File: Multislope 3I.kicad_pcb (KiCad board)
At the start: 4 copper layers, 112.5 x 56 mm, 115 parts, among them J1 INT, J10 SLOT, J11 TEST, J12 UART, J13 INPUT, J2 TEST, J3 SLOT, J4 SLOT, J5 SLOT, J6 SLOT, J7 SLOT, J8 SLOT, J9 SLOT, Q1 5551, U1 OPA21xx, U10 LM311, U11 NE5534, U12 OPA197, U13 431, U14 431, U15 MCP3202, U16 Pico, U17 LM35, U18 ADuM121N, U2 LM399, U3 CD4053B, U4 OPA1xx, U5 OPA1xx, U6 OPA1xx, U7 431, U8 431, U9 408

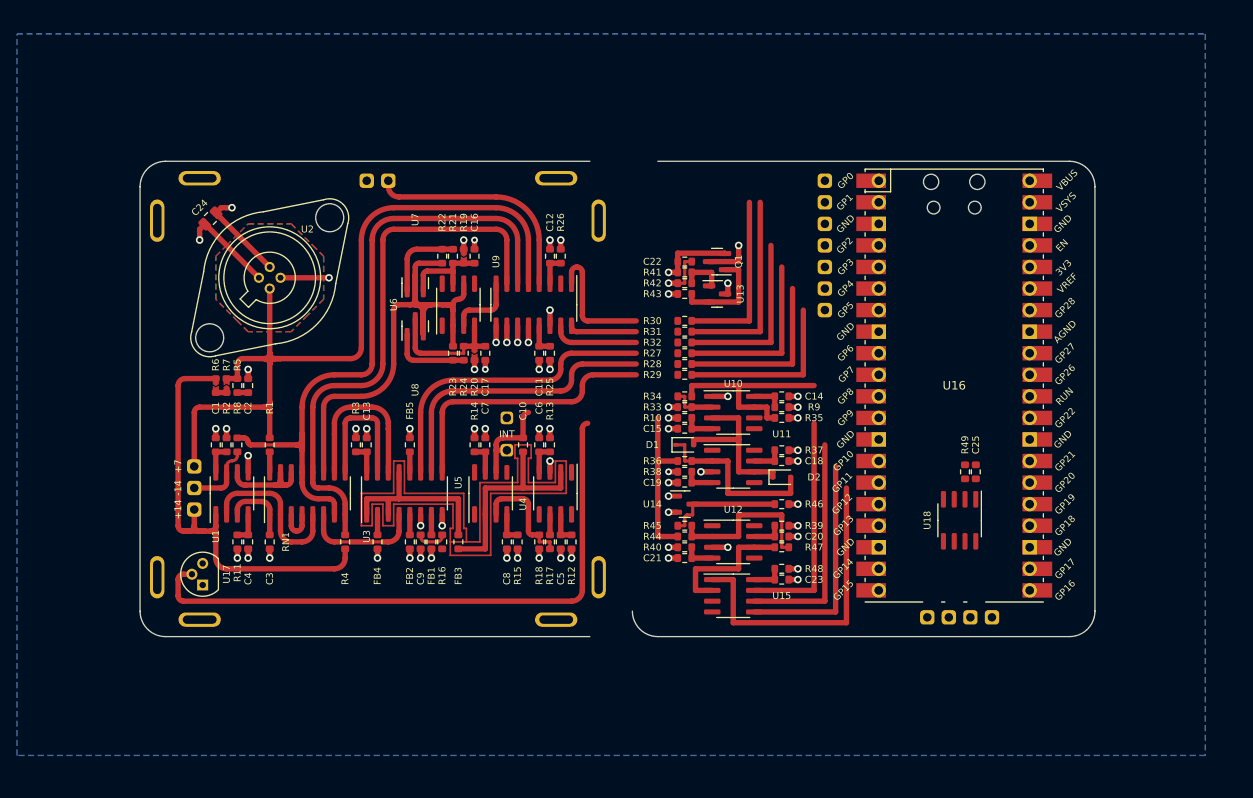
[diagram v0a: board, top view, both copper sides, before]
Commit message: PCB compact-ified
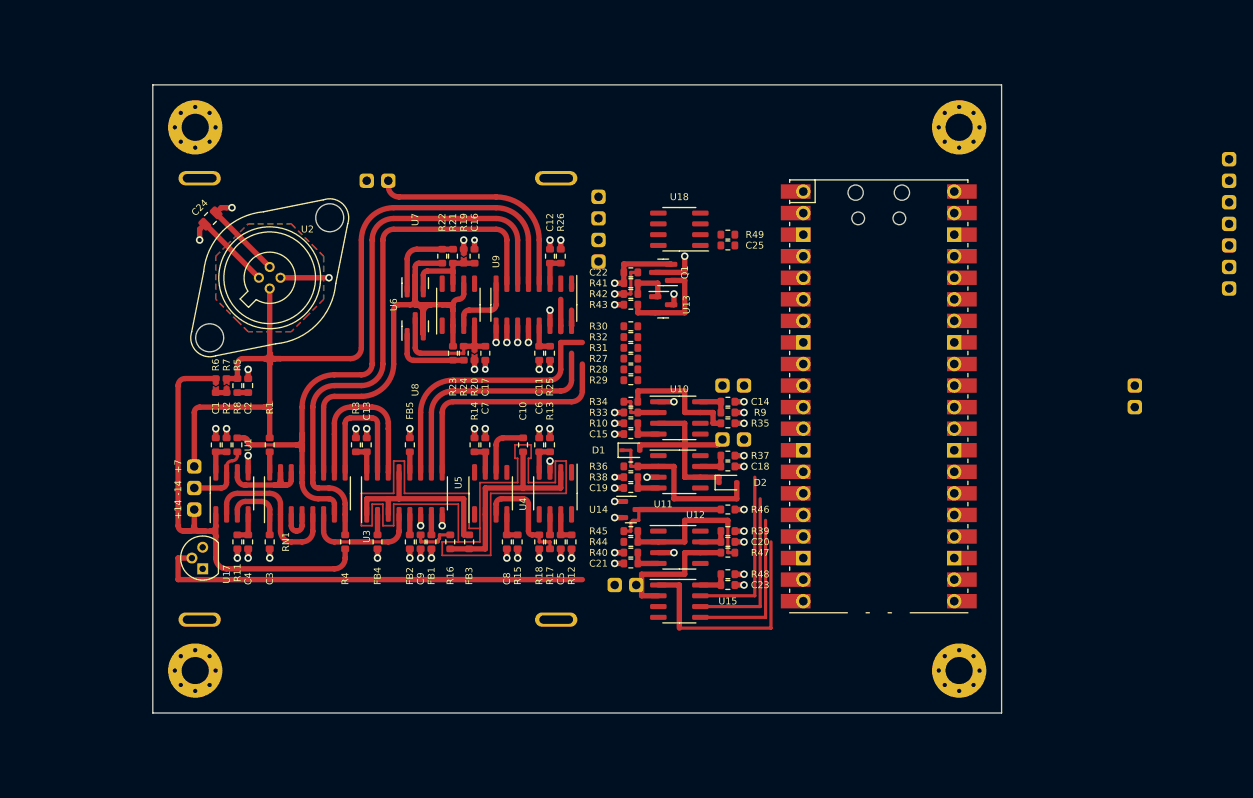
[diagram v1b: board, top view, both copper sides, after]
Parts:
- removed J10, J8: SLOT, Connector_PinHeader_2.54mm:PinHeader_1x01_P2.54mm_Vertical
- added H1: MountingHole, MountingHole:MountingHole_3.2mm_M3_Pad_Via, F.Cu at (186.0, 132.0)
- added H2: MountingHole, MountingHole:MountingHole_3.2mm_M3_Pad_Via, F.Cu at (96.0, 132.0)
- added H3: MountingHole, MountingHole:MountingHole_3.2mm_M3_Pad_Via, F.Cu at (186.0, 68.0)
- added H4: MountingHole, MountingHole:MountingHole_3.2mm_M3_Pad_Via, F.Cu at (96.0, 68.0)
- added J14: SLOPE, Connector_PinHeader_2.54mm:PinHeader_1x02_P2.54mm_Vertical, F.Cu at (158.1, 104.8)
- J1: footprint Connector_PinHeader_2.54mm:PinHeader_1x03_P2.54mm_Vertical -> Connector_PinHeader_2.54mm:PinHeader_1x02_P2.54mm_Vertical
- J3: value SLOT -> COMP; footprint Connector_PinHeader_2.54mm:PinHeader_1x01_P2.54mm_Vertical -> Connector_PinHeader_2.54mm:PinHeader_1x02_P2.54mm_Vertical
- J7: value SLOT -> SLOPE2; footprint Connector_PinHeader_2.54mm:PinHeader_1x01_P2.54mm_Vertical -> Connector_PinHeader_2.54mm:PinHeader_1x02_P2.54mm_Vertical
- R44: value 5K -> 50K
- R45: value 2K5 -> 25K
- R47: value 1K5 -> 15K
- moved J1 74.4 mm to (206.7, 98.4), turned to 0 degrees
- moved J3 69.4 mm to (158.1, 98.4)
- moved J12 62.5 mm to (143.5, 83.8), turned to 180 degrees
- moved J2 47.7 mm to (217.8, 71.8)
- moved U18 47.6 mm to (153.0, 80.0), turned to 180 degrees
- moved J7 43.1 mm to (148.0, 121.9), turned to -90 degrees
- moved C25 39.6 mm to (158.8, 81.9), turned to 180 degrees
- moved R49 39.5 mm to (158.8, 80.6), turned to 0 degrees
- moved U16 8.98 mm to (176.5, 99.7)
- moved R31 6.63 mm to (147.3, 94.0)
- moved C22 6.48 mm to (147.3, 85.1)
- moved Q1 6.48 mm to (151.1, 85.1)
- moved R43 6.48 mm to (147.3, 88.9)
- moved U13 6.48 mm to (151.1, 88.9)
- moved R41 6.48 mm to (147.3, 86.4)
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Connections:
- net Net-(D1-Pad2) renamed /SLOPE
- J2 pad 2: Net-(J2-Pad2) -> Net-(U16-Pad4)
- J2 pad 4: Net-(J2-Pad4) -> Net-(U16-Pad2)
- J3 pad 1: GND -> /COMP
- J7 pad 1: GND -> /SLOPE2
- R31 pad 2: Net-(J2-Pad2) -> Net-(U16-Pad4)
- R32 pad 2: Net-(J2-Pad4) -> Net-(U16-Pad2)
- R34 pad 2: Net-(R34-Pad2) -> /COMP
- R35 pad 1: Net-(R34-Pad2) -> /COMP
- R47 pad 2: Net-(R47-Pad2) -> /SLOPE2
- U10 pad 7: Net-(R34-Pad2) -> /COMP
- U12 pad 6: Net-(R47-Pad2) -> /SLOPE2
- U15 pad 2: Net-(R47-Pad2) -> /SLOPE2
- U16 pad 12: Net-(R34-Pad2) -> /COMP
- U16 pad 2: Net-(J2-Pad2) -> Net-(U16-Pad2)
- U16 pad 4: Net-(J2-Pad4) -> Net-(U16-Pad4)
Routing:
- net /SLOPE: track 21.3 -> 75.0 mm
- net /SLOPE2: track 0.00 -> 50.7 mm
- net +15V: track 206.7 -> 157.8 mm
- net -15V: track 253.9 -> 219.6 mm
- net Net-(R34-Pad2): track 23.7 -> 0.00 mm
- net Net-(J2-Pad2): track 23.3 -> 0.00 mm
- net /INT: track 30.1 -> 6.85 mm
- net Net-(J2-Pad6): track 20.8 -> 0.00 mm
- net Net-(J2-Pad4): track 20.8 -> 0.00 mm
- net Net-(J2-Pad1): track 20.8 -> 0.00 mm
- net Net-(J2-Pad7): track 20.8 -> 0.00 mm
- net Net-(J2-Pad5): track 20.8 -> 0.00 mm
- net Net-(U15-Pad3): track 72.5 -> 51.8 mm
- net Net-(R47-Pad2): track 16.4 -> 0.00 mm
- net /COMP: track 0.00 -> 14.9 mm
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- removed copper zone on B.Cu, net GND
- removed copper zone on In2.Cu, net GND
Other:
- board size 112.5 x 56 mm -> 100 x 74 mm

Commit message: removed redundant files
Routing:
- net /SLOPE: track 75.0 -> 26.1 mm
- net /SLOPE2: track 50.7 -> 16.4 mm
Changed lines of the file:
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@@
   (segment (start 153.67 109.22) (end 155.51 109.22) (width 0.635) (layer "F.Cu") (net 65))
   (arc (start 157.48 105.41) (mid 157.929013 105.224013) (end 158.115 104.775) (width 0.635) (layer "F.Cu") (net 65))
-  (segment (start 153.67 106.045) (end 160.655 106.045) (width 0.635) (layer "In1.Cu") (net 65))
-  (segment (start 153.67 90.17) (end 153.67 100.965) (width 0.635) (layer "In1.Cu") (net 65))
-  (segment (start 145.415 90.17) (end 153.67 90.17) (width 0.635) (layer "In1.Cu") (net 65))
-  (segment (start 153.67 100.965) (end 160.655 100.965) (width 0.635) (layer "In1.Cu") (net 65))
-  (segment (start 145.415 90.17) (end 145.415 87.63) (width 0.635) (layer "In1.Cu") (net 65))
-  (segment (start 153.67 100.965) (end 153.67 106.045) (width 0.635) (layer "In1.Cu") (net 65))
-  (segment (start 153.67 90.17) (end 153.67 81.915) (width 0.635) (layer "In1.Cu") (net 65))
   (segment (start 148.145 101.6) (end 150.56 101.6) (width 0.635) (layer "F.Cu") (net 66))
   (segment (start 146.495 100.33) (end 147.32 100.33) (width 0.381) (layer "F.Cu") (net 66))
@@
   (segment (start 155.51 118.11) (end 153.67 118.11) (width 0.635) (layer "F.Cu") (net 124))
   (segment (start 148.59 123.19) (end 150.56 123.19) (width 0.635) (layer "F.Cu") (net 124))
-  (segment (start 147.32 102.235) (end 147.32 108.585) (width 0.635) (layer "In1.Cu") (net 124))
-  (segment (start 145.415 102.235) (end 147.32 102.235) (width 0.635) (layer "In1.Cu") (net 124))
-  (segment (start 147.32 108.585) (end 145.415 108.585) (width 0.635) (layer "In1.Cu") (net 124))
-  (segment (start 145.415 117.475) (end 147.32 117.475) (width 0.635) (layer "In1.Cu") (net 124))
-  (segment (start 147.32 117.475) (end 147.32 112.395) (width 0.635) (layer "In1.Cu") (net 124))
-  (segment (start 160.655 112.395) (end 147.32 112.395) (width 0.635) (layer "In1.Cu") (net 124))
-  (segment (start 147.32 112.395) (end 147.32 108.585) (width 0.635) (layer "In1.Cu") (net 124))
   (segment (start 93.98 118.745) (end 93.98 121.285) (width 0.635) (layer "F.Cu") (net 125))
   (segment (start 95.61 118.745) (end 93.98 118.745) (width 0.635) (layer "F.Cu") (net 125))

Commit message: pcb completed
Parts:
- added C26: 1uf, Resistor_SMD:R_0603_1608Metric, F.Cu at (177.8, 118.7)
- added J10: PWR, Connector_PinHeader_2.54mm:PinHeader_1x04_P2.54mm_Vertical, F.Cu at (166.1, 127.3)
- added J8: PWR, Connector_PinHeader_2.54mm:PinHeader_1x03_P2.54mm_Vertical, F.Cu at (158.1, 67.9)
- R41: value 10R -> 2K4
- R42: value 10R -> 7K5
- R43: value 10R -> 10K
- moved J1 62.0 mm to (145.4, 108.0), turned to 90 degrees
- moved J2 57.3 mm to (160.7, 75.6)
- moved J12 50.0 mm to (181.6, 116.2), turned to -90 degrees
- moved U18 38.3 mm to (177.8, 109.2), turned to -90 degrees
- moved R49 30.2 mm to (178.4, 103.5), turned to 90 degrees
- moved C25 30.1 mm to (179.7, 103.5), turned to -90 degrees
- moved C22 6.98 mm to (147.3, 78.1)
- moved Q1 6.98 mm to (151.1, 78.1)
- moved R41 6.98 mm to (147.3, 79.4)
- moved R42 6.98 mm to (147.3, 80.6)
- moved R43 6.98 mm to (147.3, 81.9)
- moved U13 6.98 mm to (151.1, 81.9)
- moved J13 6.48 mm to (117.5, 67.9)
- moved U14 6.29 mm to (151.8, 108.6)
- moved C15 4.45 mm to (147.3, 99.7)
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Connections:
- J2 pad 2: Net-(U16-Pad4) -> Net-(J2-Pad2)
- J2 pad 4: Net-(U16-Pad2) -> Net-(R31-Pad2)
- R31 pad 2: Net-(U16-Pad4) -> Net-(R31-Pad2)
- R32 pad 2: Net-(U16-Pad2) -> Net-(J2-Pad2)
- U16 pad 11: unconnected-(U16-Pad11) -> Net-(U16-Pad11)
- U16 pad 12: /COMP -> Net-(U18-Pad2)
- U16 pad 13: unconnected-(U16-Pad13) -> GND
- U16 pad 18: unconnected-(U16-Pad18) -> GND
- U16 pad 2: Net-(U16-Pad2) -> Net-(J2-Pad2)
- U16 pad 21: Net-(U16-Pad21) -> unconnected-(U16-Pad21)
- U16 pad 22: Net-(U16-Pad22) -> unconnected-(U16-Pad22)
- U16 pad 23: unconnected-(U16-Pad23) -> GND
- U16 pad 28: unconnected-(U16-Pad28) -> GND
- U16 pad 3: unconnected-(U16-Pad3) -> GND
- U16 pad 33: unconnected-(U16-Pad33) -> GND
- U16 pad 38: unconnected-(U16-Pad38) -> GND
- U16 pad 4: Net-(U16-Pad4) -> Net-(R31-Pad2)
- U16 pad 8: unconnected-(U16-Pad8) -> GND
- U16 pad 9: unconnected-(U16-Pad9) -> /COMP
- U18 pad 2: Net-(U16-Pad22) -> Net-(U18-Pad2)
- U18 pad 3: Net-(U16-Pad21) -> Net-(U16-Pad11)
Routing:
- net +3V3: track 13.3 -> 255.5 mm, vias 5 -> 6
- net +15V: track 157.8 -> 278.0 mm
- net -15V: track 219.6 -> 319.9 mm
- net (no net): track 0.00 -> 48.3 mm
- net /INT: track 6.85 -> 34.0 mm
- net Net-(J2-Pad1): track 0.00 -> 27.0 mm
- net Net-(J2-Pad2): track 0.00 -> 26.2 mm
- net Net-(R31-Pad2): track 0.00 -> 23.1 mm
- net Net-(J2-Pad5): track 0.00 -> 22.6 mm
- net /COMP: track 14.9 -> 37.2 mm
- net Net-(J2-Pad6): track 0.00 -> 22.1 mm
- net Net-(J2-Pad7): track 0.00 -> 21.6 mm
- net Net-(U18-Pad2): track 0.00 -> 15.3 mm
- net Net-(U16-Pad11): track 0.00 -> 13.4 mm
- net GND: track 178.1 -> 189.5 mm, vias 44 -> 46
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- added copper zone on B.Cu, net GND
- added copper zone on In1.Cu, net GND
- added copper zone on In2.Cu, net GND
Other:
- outline, holes or cut-outs redrawn
- board text added: "+15"
- board text added: "+3.3V"
- board text added: "-15"
- board text added: "GND"
- board text added: "IN"
- board text added: "NNNI 1722 Multislope 3I"
- board text added: "RX"
- board text added: "TX"
- board text added: "VCC"

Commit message: 'final' PCB
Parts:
- added C27: 1uf, Resistor_SMD:R_0603_1608Metric, F.Cu at (175.9, 91.4)
- added Q2: 5551, Package_TO_SOT_SMD:SOT-23, F.Cu at (179.7, 91.4)
- added R50: 10K, Resistor_SMD:R_0603_1608Metric, F.Cu at (175.9, 92.7)
- added R51: 10K, Resistor_SMD:R_0603_1608Metric, F.Cu at (175.9, 94.0)
- added R52: 10K, Resistor_SMD:R_0603_1608Metric, F.Cu at (175.9, 95.2)
- added U19: 431, Package_TO_SOT_SMD:SOT-23, F.Cu at (179.7, 95.2)
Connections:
- U16 pad 39: unconnected-(U16-Pad39) -> +5V
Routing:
- net +15V: track 278.0 -> 367.7 mm, vias 10 -> 12
- net -15V: track 319.9 -> 345.5 mm
- net +5V: track 0.00 -> 25.1 mm
- net +3V3: track 255.5 -> 279.9 mm
- net Net-(Q2-Pad1): track 0.00 -> 10.6 mm
- net GND: track 189.5 -> 196.4 mm, vias 46 -> 48
- net Net-(R50-Pad1): track 0.00 -> 5.07 mm
- added copper zone on In1.Cu, net (none)
- added copper zone on In2.Cu, net (none)
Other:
- board text added: "."

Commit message: minor mistakes fixed
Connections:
- J8 pad 1: unconnected-(J8-Pad1) -> +15V
- J8 pad 3: unconnected-(J8-Pad3) -> -15V
- U9 pad 2: unconnected-(U9-Pad2) -> +3V3
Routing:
- net +3V3: track 279.9 -> 292.1 mm, vias 6 -> 7

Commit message: pcb final touches
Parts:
- removed Q1, Q2: 5551, Package_TO_SOT_SMD:SOT-23
- removed R41: 2K4, Resistor_SMD:R_0603_1608Metric
- removed R42: 7K5, Resistor_SMD:R_0603_1608Metric
- removed R43, R50, R51, R52: 10K, Resistor_SMD:R_0603_1608Metric
- removed U13, U19: 431, Package_TO_SOT_SMD:SOT-23
- added C28: 1uf, Resistor_SMD:R_0603_1608Metric, F.Cu at (150.5, 83.2)
- added C29: 1uf, Resistor_SMD:R_0603_1608Metric, F.Cu at (150.5, 81.9)
- added C30: 1uf, Resistor_SMD:R_0603_1608Metric, F.Cu at (99.7, 116.8)
- added J15: PWR, Connector_PinHeader_2.54mm:PinHeader_1x03_P2.54mm_Vertical, F.Cu at (153.0, 73.7)
- added SW1: RST, Button_Switch_SMD:SW_Push_1P1T_NO_CK_KMR2, F.Cu at (164.5, 70.5)
- added U20: HT7533, Package_TO_SOT_SMD:SOT-89-3, F.Cu at (146.4, 78.1)
- added U21: HT7550, Package_TO_SOT_SMD:SOT-89-3, F.Cu at (146.4, 83.2)
- moved C27 29.3 mm to (150.5, 76.8)
- moved J2 3.81 mm to (164.5, 75.6)
- moved C22 3.18 mm to (150.5, 78.1)
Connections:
- C22 pad 1: +3V3 -> +15V
- C27 pad 1: +5V -> +3V3
- U16 pad 30: unconnected-(U16-Pad30) -> Net-(SW1-Pad2)
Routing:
- net +3V3: track 292.1 -> 442.4 mm, vias 7 -> 8
- net +15V: track 367.7 -> 290.4 mm, vias 12 -> 24
- net Net-(SW1-Pad2): track 0.00 -> 54.8 mm, vias 0 -> 1
- net +5V: track 25.1 -> 60.2 mm, vias 0 -> 1
- net -15V: track 345.5 -> 358.2 mm
- net Net-(Q1-Pad1): track 10.6 -> 0.00 mm
- net Net-(Q2-Pad1): track 10.6 -> 0.00 mm
- net Net-(R41-Pad1): track 5.21 -> 0.00 mm
- net Net-(R50-Pad1): track 5.07 -> 0.00 mm
- net GND: track 196.4 -> 199.1 mm, vias 48 -> 52
- net Net-(J2-Pad1): track 27.0 -> 25.2 mm
- net Net-(J2-Pad2): track 26.2 -> 24.7 mm
- added copper zone on B.Cu, net +15V
- added copper zone on F.Cu, net +15V
- added copper zone on In1.Cu, net +15V
- added copper zone on In2.Cu, net +15V
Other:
- board text added: "+3V3"
- board text added: "+5V"

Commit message: Changes
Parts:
- added R41: 0R, 0603 Jumper:0603 Jumper, F.Cu at (147.3, 118.7)
- added R42: 0R, 0603 Jumper:0603 Jumper, F.Cu at (147.3, 120.0)
- R44: value 50K -> 51K
- R45: value 25K -> 24K
- moved J7 0.63 mm to (148.0, 116.8)
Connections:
- net Net-(R27-Pad1) renamed /PWMA
- net Net-(R28-Pad1) renamed /PWMB
- net Net-(R29-Pad1) renamed /MEAS
- U15 pad 2: /SLOPE2 -> Net-(U15-Pad2)
- U15 pad 5: Net-(U15-Pad5) -> Net-(U16-Pad15)
- U15 pad 6: Net-(U15-Pad6) -> Net-(U16-Pad16)
- U16 pad 15: Net-(U15-Pad6) -> Net-(U16-Pad15)
- U16 pad 16: Net-(U15-Pad5) -> Net-(U16-Pad16)
- U17 pad 2: Net-(U15-Pad3) -> Net-(U17-Pad2)
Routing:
- net Net-(U15-Pad3): track 60.8 -> 2.41 mm
- net Net-(U17-Pad2): track 0.00 -> 57.2 mm
- net Net-(U16-Pad16): track 0.00 -> 25.3 mm
- net Net-(U16-Pad15): track 0.00 -> 20.6 mm
- net Net-(U15-Pad6): track 19.7 -> 0.00 mm
- net Net-(U15-Pad5): track 18.9 -> 0.00 mm
- net /INT: track 34.0 -> 38.6 mm
- net Net-(U15-Pad2): track 0.00 -> 2.41 mm
- net Net-(U15-Pad1): track 26.6 -> 28.7 mm
- net /SLOPE2: track 16.2 -> 14.2 mm
- net GND: track 199.1 -> 198.1 mm
- net +3V3: track 442.4 -> 443.0 mm
